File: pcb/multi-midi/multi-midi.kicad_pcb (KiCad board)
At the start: 2 copper layers, 101.2 x 71.1 mm, 60 parts, among them J1 DIN-5_180degree, J10 Conn_01x04_Male, J11 Conn_01x04_Male, J12 Barrel_Jack_Switch, J13 Conn_01x03_Male, J2 DIN-5_180degree, J3 DIN-5_180degree, J4 DIN-5_180degree, J5 DIN-5_180degree, J6 DIN-5_180degree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

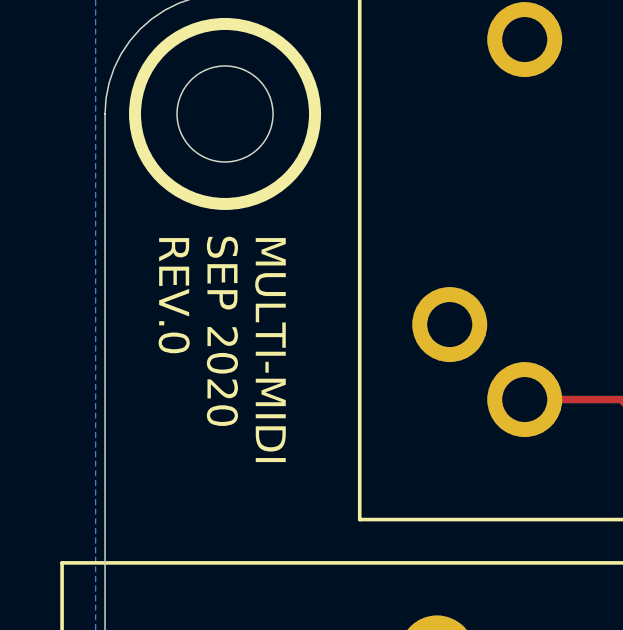
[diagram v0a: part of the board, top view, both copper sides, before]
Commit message: Fix board-level caps value, part No.; update to rev1
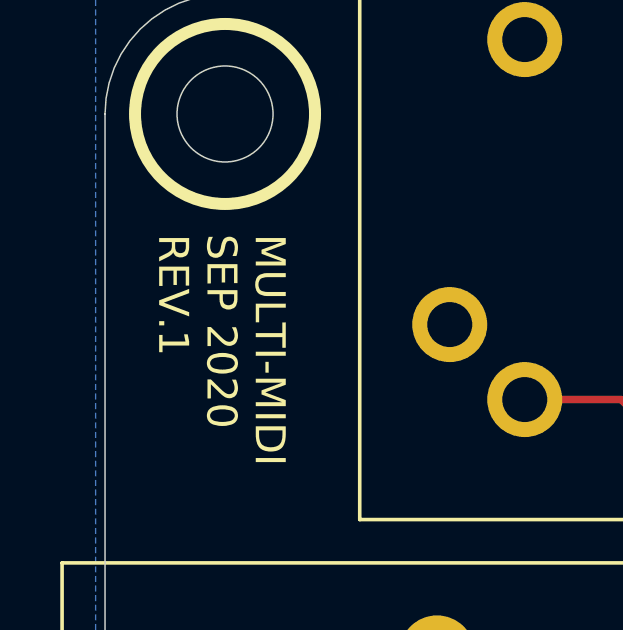
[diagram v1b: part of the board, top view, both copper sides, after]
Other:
- board text added: "MULTI-MIDI SEP 2020 REV.1"
- board text removed: "MULTI-MIDI SEP 2020 REV.0"
